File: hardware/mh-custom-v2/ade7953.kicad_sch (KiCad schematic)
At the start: 58 parts, among them U2 ADE7953xCP, Y1 3.58MHz

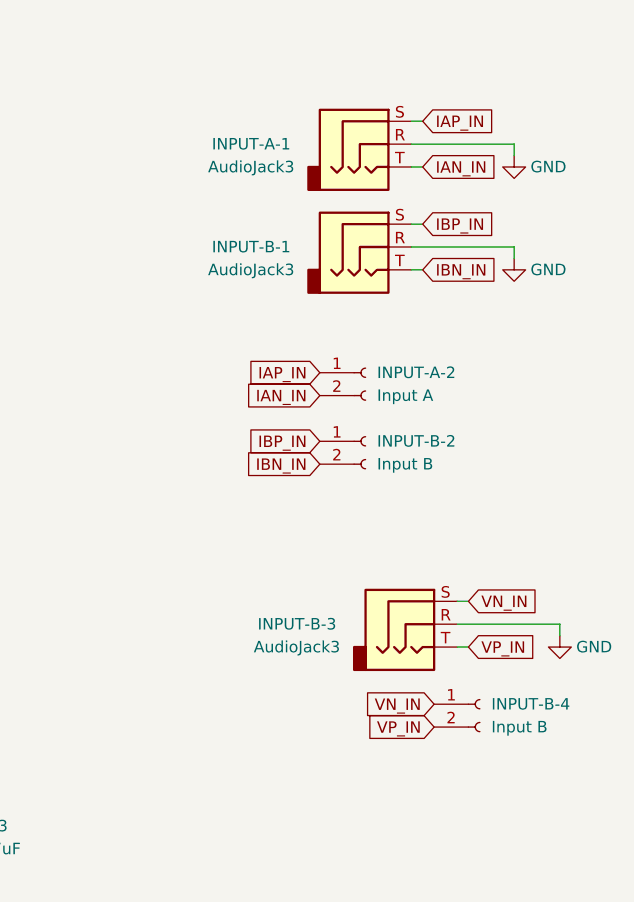
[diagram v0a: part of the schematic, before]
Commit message: low-voltage side of V2 board rebuilt. Started on high-voltage side
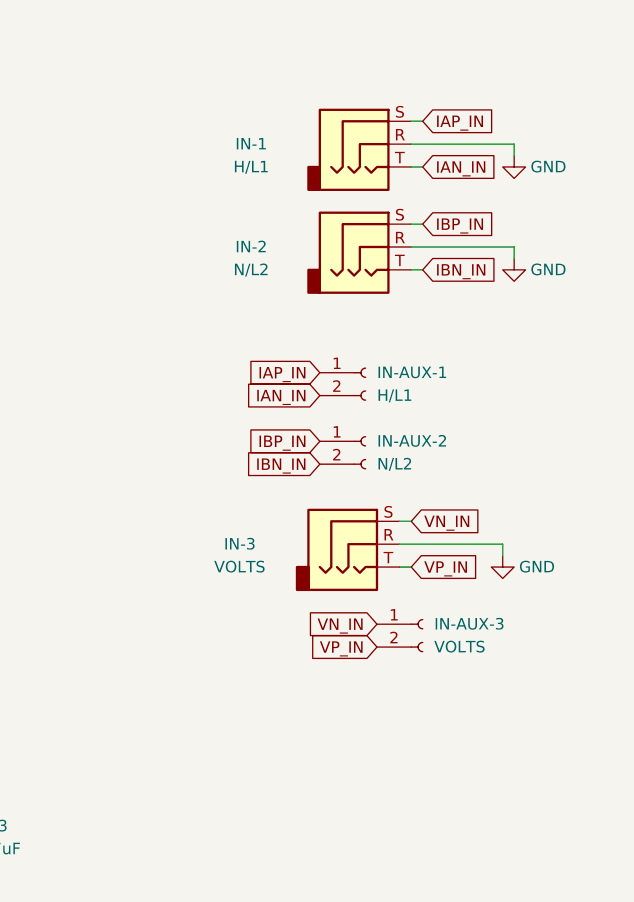
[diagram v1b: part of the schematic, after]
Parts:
- removed INPUT-B-1, INPUT-B-3: AudioJack3, Connector_Audio:Jack_3.5mm_CUI_SJ1-3523N_Horizontal, symbol Connector:AudioJack3
- added IN-2: N/L2, Connector_Audio:Jack_3.5mm_CUI_SJ-3523-SMT_Horizontal, symbol Connector:AudioJack3
- added IN-3: VOLTS, Connector_Audio:Jack_3.5mm_CUI_SJ-3523-SMT_Horizontal, symbol Connector:AudioJack3
- C10, C11, C12, C13, C15, C16, C17, C20, C21, C22, C3, C4, C5, C6, C7, C8, C9: footprint Capacitor_SMD:C_0201_0603Metric -> LED_SMD:LED_0603_1608Metric
- IN-1: renamed from INPUT-A-1; value AudioJack3 -> H/L1; footprint Connector_Audio:Jack_3.5mm_CUI_SJ1-3523N_Horizontal -> Connector_Audio:Jack_3.5mm_CUI_SJ-3523-SMT_Horizontal; JLCPCB Part # (none) -> C18594
- IN-AUX-1: renamed from INPUT-A-2; value Input A -> H/L1
- IN-AUX-2: renamed from INPUT-B-2; value Input B -> N/L2
- IN-AUX-3: renamed from INPUT-B-4; value Input B -> VOLTS
- JP12, JP6, JP7: footprint (none) -> Jumper:SolderJumper-2_P1.3mm_Bridged_RoundedPad1.0x1.5mm
- R10, R11, R12, R13, R14, R15, R16, R17, R18, R19, R20, R21, R22, R23, R24, R25, R9: footprint Resistor_SMD:R_0201_0603Metric -> Resistor_SMD:R_0603_1608Metric
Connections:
- net GND: now also IN-2.R, IN-3.R
- net IBN_IN: now also IN-2.T
- net IBP_IN: now also IN-2.S
- net VN_IN: now also IN-3.S
- net VP_IN: now also IN-3.T
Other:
- moved on the sheet: IN-AUX-3

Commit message: approaching ordering from JLCPCB
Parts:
- C10, C11, C12, C3, C4, C5, C6, C7, C8, C9: JLCPCB Part # (none) -> C21117
- C13, C16, C17, C22: JLCPCB Part # (none) -> C14663
- C14: JLCPCB Part # (none) -> C88726
- C15: JLCPCB Part # (none) -> C15849
- C18, C19, C23: JLCPCB Part # (none) -> C88759
- C20, C21: JLCPCB Part # (none) -> C1648
- IN-1, IN-2, IN-3: footprint Connector_Audio:Jack_3.5mm_CUI_SJ-3523-SMT_Horizontal -> Connector_Audio:Jack_3.5mm_CUI_SJ1-3525N_Horizontal; JLCPCB Part # C18594 -> C692542
- R10, R11, R12, R9: JLCPCB Part # (none) -> C22775
- R13, R19: JLCPCB Part # (none) -> C131054
- R14, R15, R16, R17, R18, R20, R21: JLCPCB Part # (none) -> C21190
- R22, R23, R24, R25: JLCPCB Part # (none) -> C25804
- U2: JLCPCB Part # (none) -> C515890
- Y1: JLCPCB Part # (none) -> C2826865
